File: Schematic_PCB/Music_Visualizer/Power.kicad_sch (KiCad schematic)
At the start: 16 parts, among them J2 PJ-079BH, Q1 DMP2123LQ-7, SW2 SW_SPST, U8 LT1054, U9 MC78L05_TO92

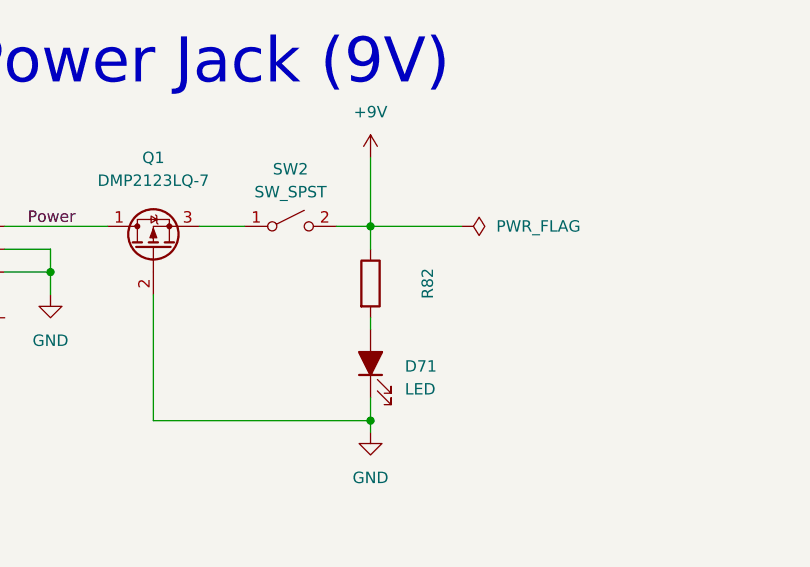
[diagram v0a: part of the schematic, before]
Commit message: Added 4th op amp in each LM324 IC as a voltage follower (buffer) for each spectrum filter in the schematic
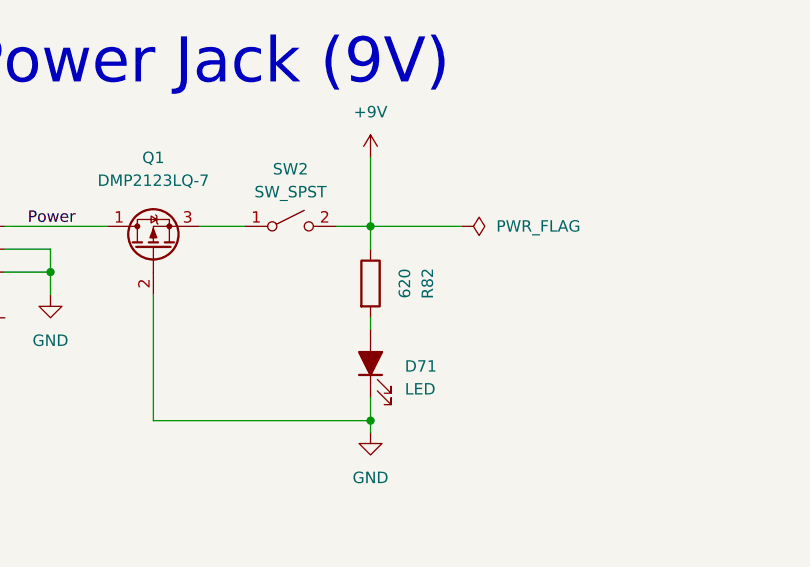
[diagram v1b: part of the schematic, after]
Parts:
- R82: value (none) -> 620; footprint (none) -> Resistor_SMD:R_0603_1608Metric_Pad0.98x0.95mm_HandSolder
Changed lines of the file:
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@@
     (in_bom yes) (on_board yes) (fields_autoplaced)
     (property "Reference" "R82" (id 0) (at 91.44 58.42 90))
-    (property "Value" "" (id 1) (at 88.9 58.42 90))
-    (property "Footprint" "" (id 2) (at 83.312 58.42 90)
+    (property "Value" "620" (id 1) (at 88.9 58.42 90))
+    (property "Footprint" "Resistor_SMD:R_0603_1608Metric_Pad0.98x0.95mm_HandSolder" (id 2) (at 83.312 58.42 90)
       (effects (font (size 1.27 1.27)) hide)
     )

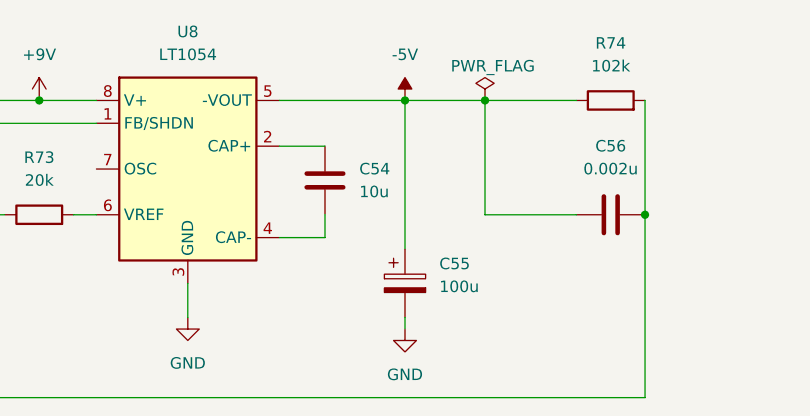
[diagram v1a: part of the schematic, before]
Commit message: Re-oriented C55 (The 100uF capacitor) so that the positive terminal is connected to ground and the negative terminal is connected to -5V in the schematic and PCB layout
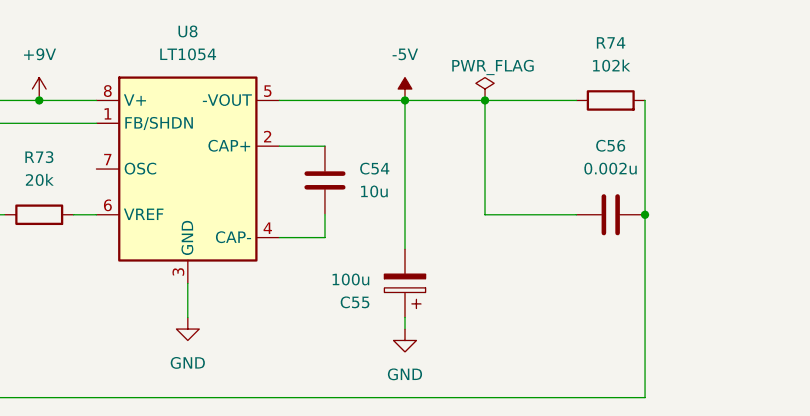
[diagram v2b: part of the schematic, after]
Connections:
- net -5V: now also C55.2; no longer C55.1
- net GND: now also C55.1; no longer C55.2
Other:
- moved on the sheet: C55
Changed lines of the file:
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@@
     (pin "1")
   )
-  (symbol (lib_id "Device:C_Polarized") (at 129.54 146.05 0) (unit 1)
+  (symbol (lib_id "Device:C_Polarized") (at 129.54 146.05 180) (unit 1)
     (in_bom yes) (on_board yes) (fields_autoplaced)
-    (property "Reference" "C55" (id 0) (at 133.35 143.8909 0)
+    (property "Reference" "C55" (id 0) (at 125.73 148.2091 0)
       (effects (font (size 1.27 1.27)) (justify left))
     )
-    (property "Value" "100u" (id 1) (at 133.35 146.4309 0)
+    (property "Value" "100u" (id 1) (at 125.73 145.6691 0)
       (effects (font (size 1.27 1.27)) (justify left))
     )
-    (property "Footprint" "Capacitor_THT:C_Radial_D5.0mm_H5.0mm_P2.00mm" (id 2) (at 130.5052 149.86 0)
+    (property "Footprint" "Capacitor_THT:C_Radial_D5.0mm_H5.0mm_P2.00mm" (id 2) (at 128.5748 142.24 0)
       (effects (font (size 1.27 1.27)) hide)
     )

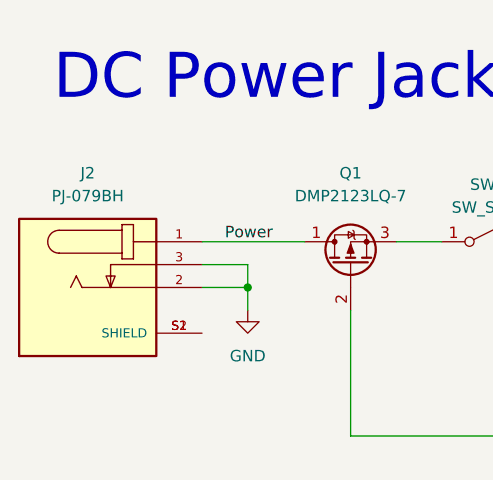
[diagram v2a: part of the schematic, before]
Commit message: Moved DC power jack symbol from global library to project specific library
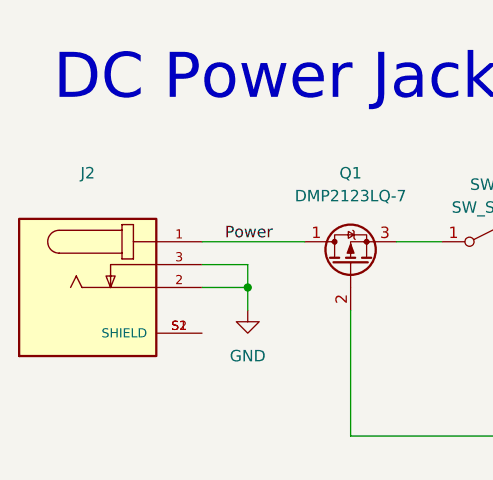
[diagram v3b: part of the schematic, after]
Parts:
- J2: value PJ-079BH -> (none); symbol DC_Power_Jack _PJ_070BH:PJ-079BH -> DC_Power_Jack_PJ-079BH:PJ-079BH
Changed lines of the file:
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@@
     (pin "2")
   )
-  (symbol (lib_id "DC_Power_Jack _PJ_070BH:PJ-079BH") (at 31.75 57.15 0) (unit 1)
+  (symbol (lib_id "DC_Power_Jack_PJ-079BH:PJ-079BH") (at 31.75 57.15 0) (unit 1)
     (in_bom yes) (on_board yes) (fields_autoplaced)
     (property "Reference" "J2" (id 0) (at 31.75 44.45 0))
-    (property "Value" "PJ-079BH" (id 1) (at 31.75 46.99 0))
+    (property "Value" "" (id 1) (at 31.75 46.99 0))
     (property "Footprint" "CUI_PJ-079BH" (id 2) (at 31.75 57.15 0)
       (effects (font (size 1.27 1.27)) (justify left bottom) hide)
     )
-    (property "Datasheet" "" (id 3) (at 31.75 57.15 0)
+    (property "Datasheet" "~" (id 3) (at 31.75 57.15 0)
       (effects (font (size 1.27 1.27)) (justify left bottom) hide)
     )

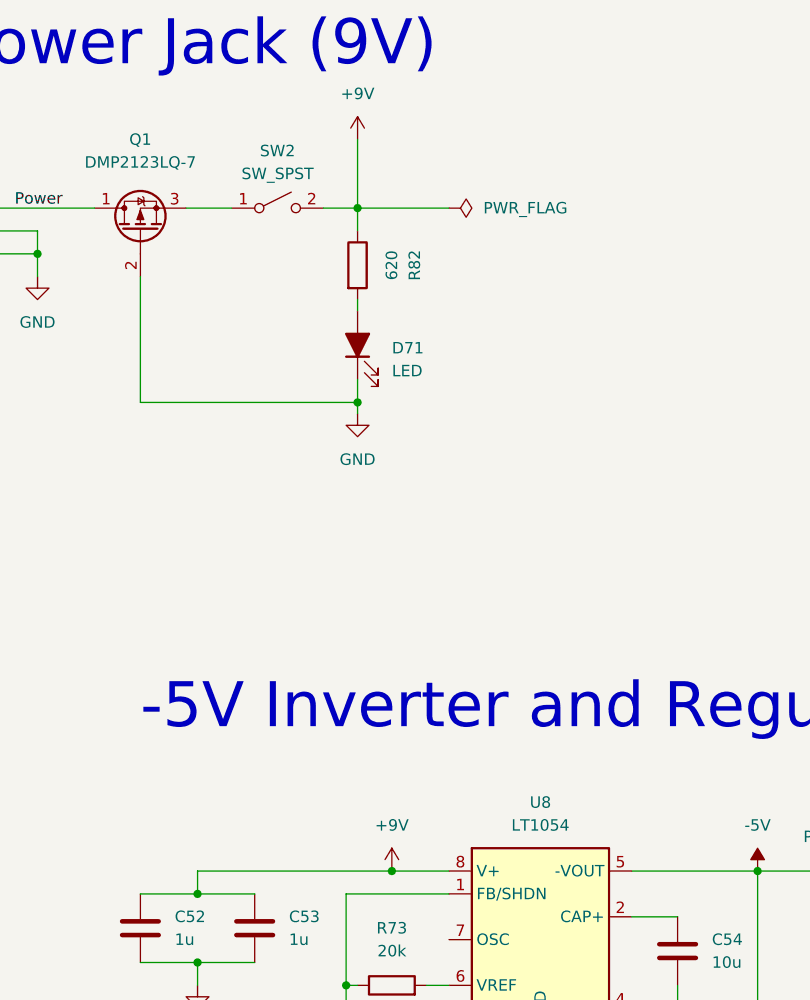
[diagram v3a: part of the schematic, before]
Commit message: Delete unneeded .step (3D-model), .kicad_mod (footprint) and .lib (schematic symbol) files in Project Library folder (AGAIN)
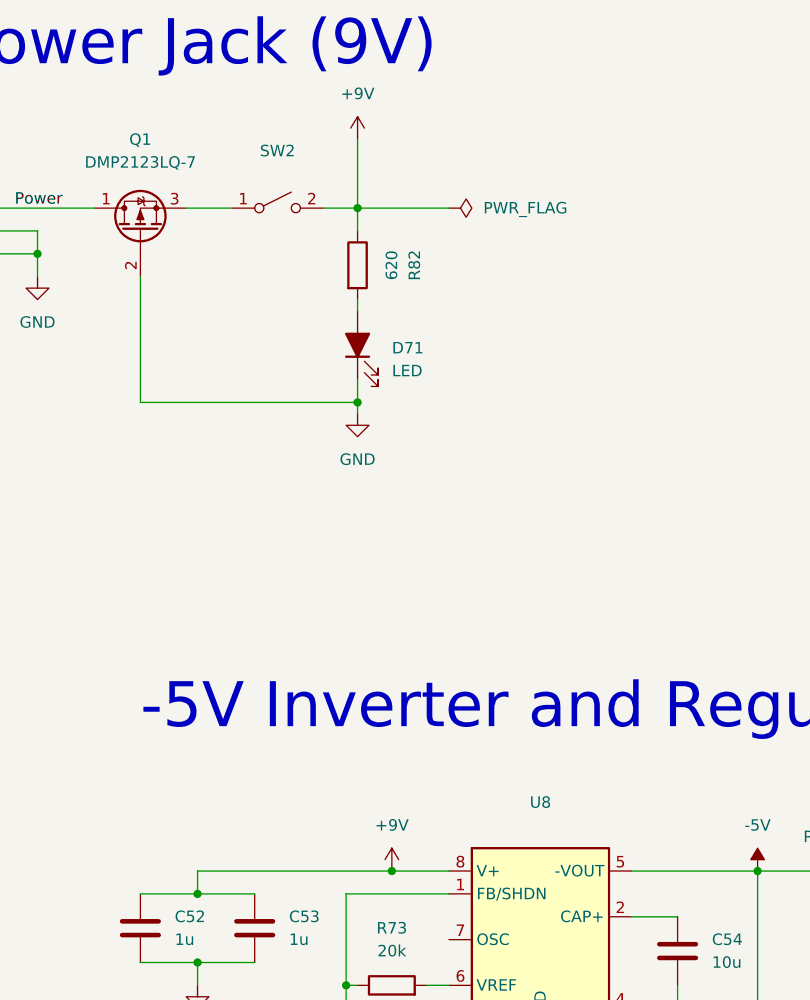
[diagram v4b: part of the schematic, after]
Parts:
- SW2: value SW_SPST -> (none); footprint PW_On_Off_Switch:E-SWITCH_RR511D1121 -> (none)
- U8: value LT1054 -> (none); footprint LT1054_PDIP_Lin_Reg:DIP794W45P254L959H508Q8 -> (none)
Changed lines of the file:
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@@
     (in_bom yes) (on_board yes) (fields_autoplaced)
     (property "Reference" "SW2" (id 0) (at 76.2 45.72 0))
-    (property "Value" "SW_SPST" (id 1) (at 76.2 48.26 0))
-    (property "Footprint" "PW_On_Off_Switch:E-SWITCH_RR511D1121" (id 2) (at 76.2 52.07 0)
+    (property "Value" "" (id 1) (at 76.2 48.26 0))
+    (property "Footprint" "" (id 2) (at 76.2 52.07 0)
       (effects (font (size 1.27 1.27)) hide)
     )
@@
     (in_bom yes) (on_board yes) (fields_autoplaced)
     (property "Reference" "U8" (id 0) (at 105.41 118.11 0))
-    (property "Value" "LT1054" (id 1) (at 105.41 120.65 0))
-    (property "Footprint" "LT1054_PDIP_Lin_Reg:DIP794W45P254L959H508Q8" (id 2) (at 107.95 135.89 0)
+    (property "Value" "" (id 1) (at 105.41 120.65 0))
+    (property "Footprint" "" (id 2) (at 107.95 135.89 0)
       (effects (font (size 1.27 1.27)) hide)
     )

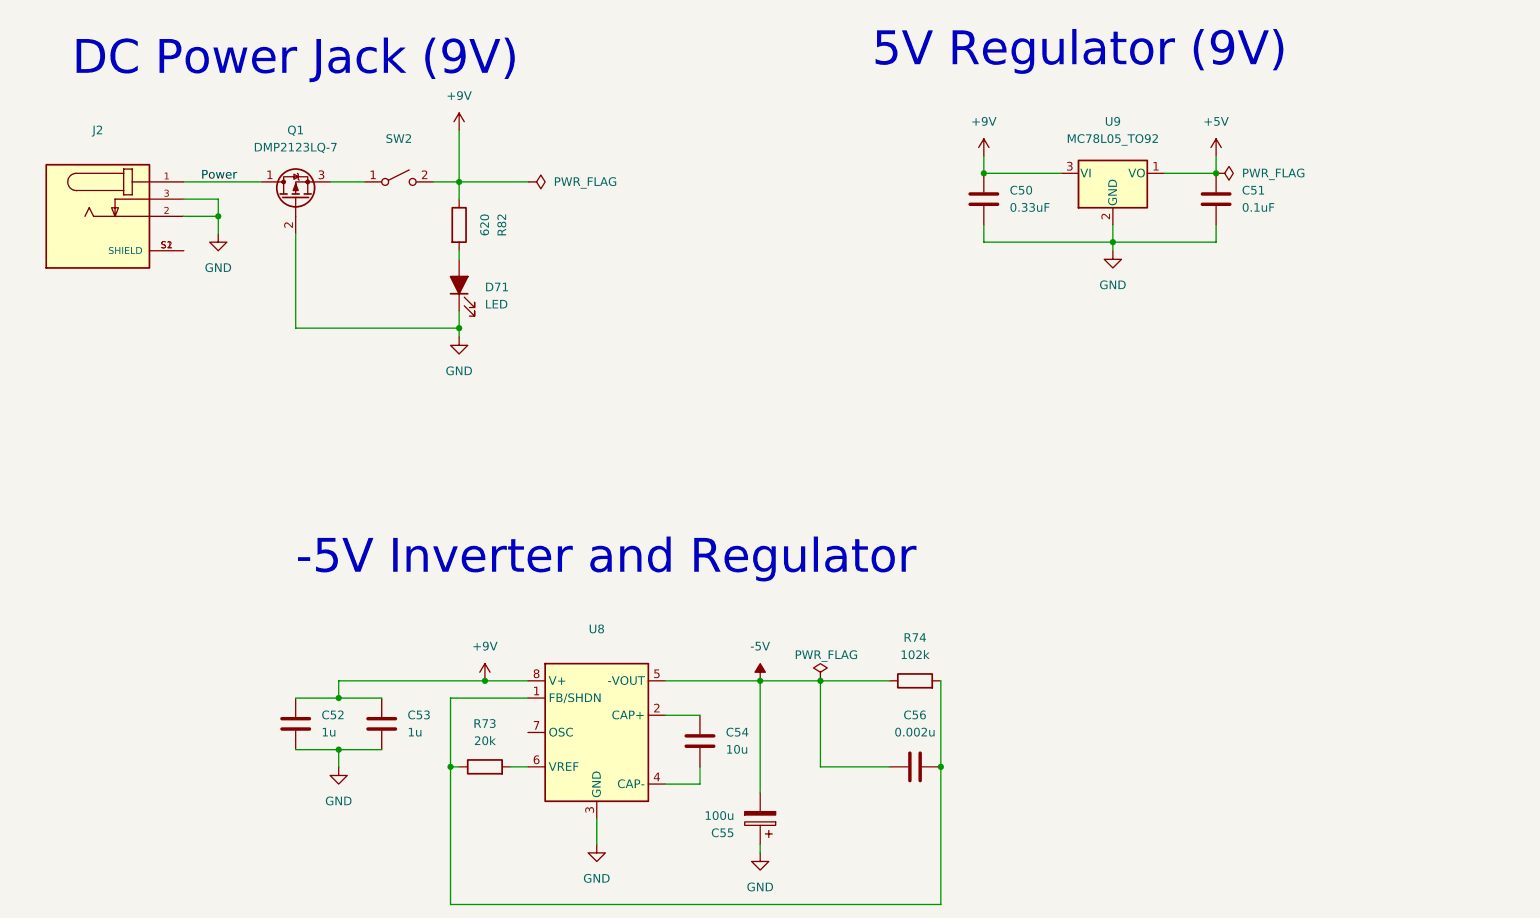
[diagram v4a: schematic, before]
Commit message: Rearraged Power circuitry schematic and made the paper size custom: 180W x 250H
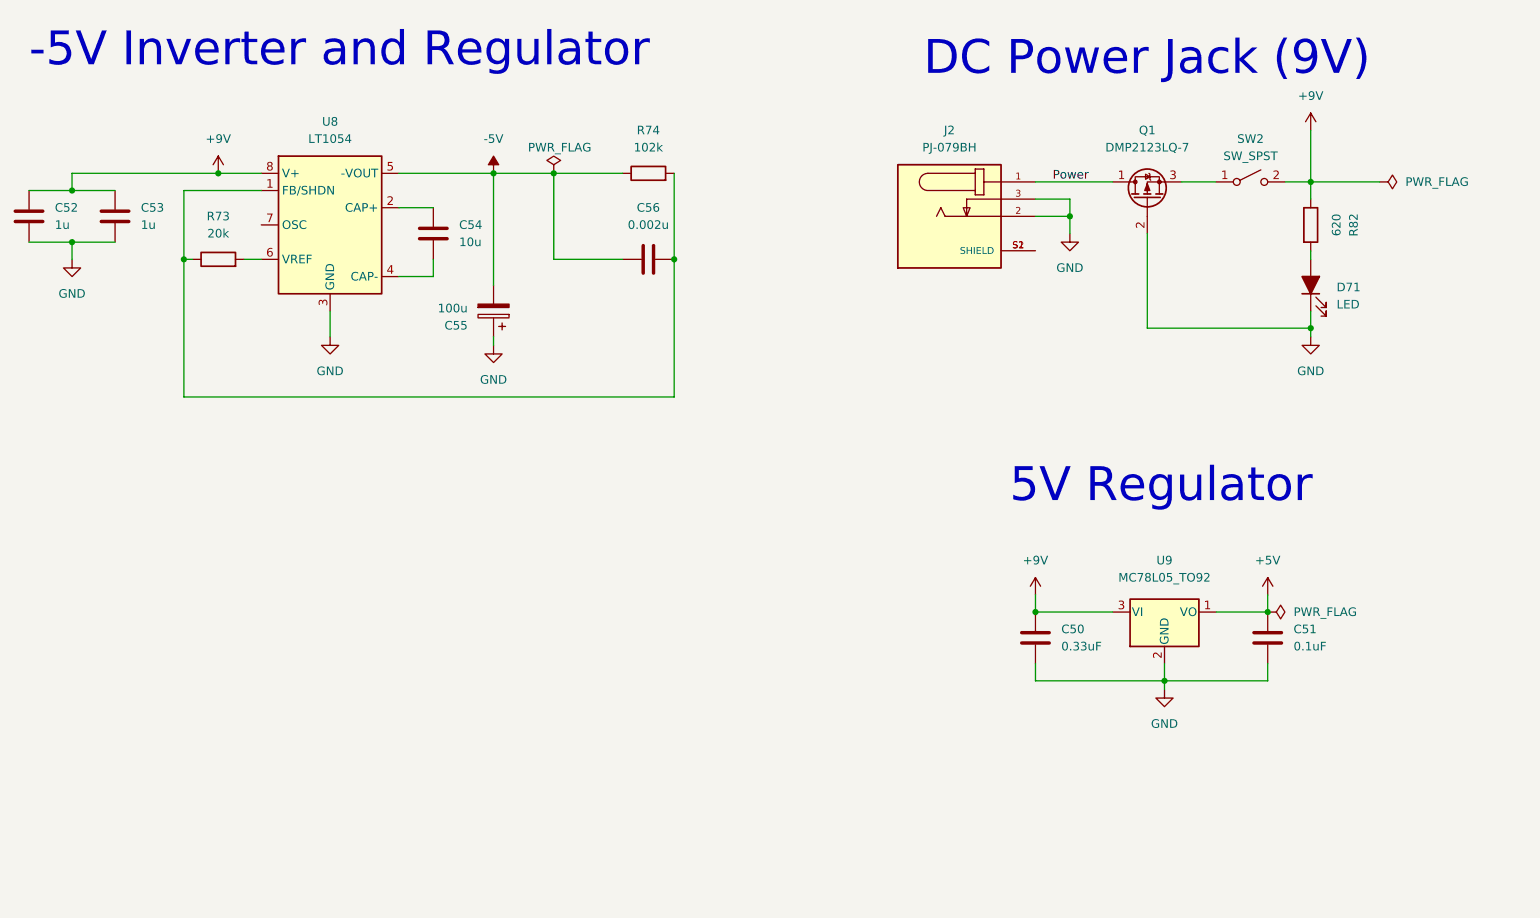
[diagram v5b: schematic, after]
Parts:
- J2: value (none) -> PJ-079BH
- SW2: value (none) -> SW_SPST; footprint (none) -> PW_On_Off_Switch:E-SWITCH_RR511D1121
- U8: value (none) -> LT1054; footprint (none) -> LT1054_PDIP_Lin_Reg:DIP794W45P254L959H508Q8
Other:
- note added: "5V Regulator"
- note removed: "5V Regulator (9V)"
- moved on the sheet: C50, C51, C52, C53, C54, C55, C56, D71, J2, Q1, R73, R74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
